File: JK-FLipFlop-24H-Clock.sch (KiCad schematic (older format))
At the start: 78 parts, among them J1 Screw_Terminal_01x02, Q1 2N3904, SW1 RESET, SW2 SET MIN, SW3 SET SEC, SW4 SET HOUR, U1 74HC109, U10 74HC00, U11 74HC00, U12 74HC00, U13 74HC00, U14 74HC00, U15 74HC00, U16 74HC00, U17 74HC109, U18 74HC109, U19 74HC109, U2 74HC109, U20 SG-3032JC, U21 74HC14, U22 74HC4040, U26 74HC4040, U3 74HC109, U4 L7805, U5 74HC109, U6 74HC109, U7 74HC109, U8 LP2950-3.0_TO92, U9 74HC109

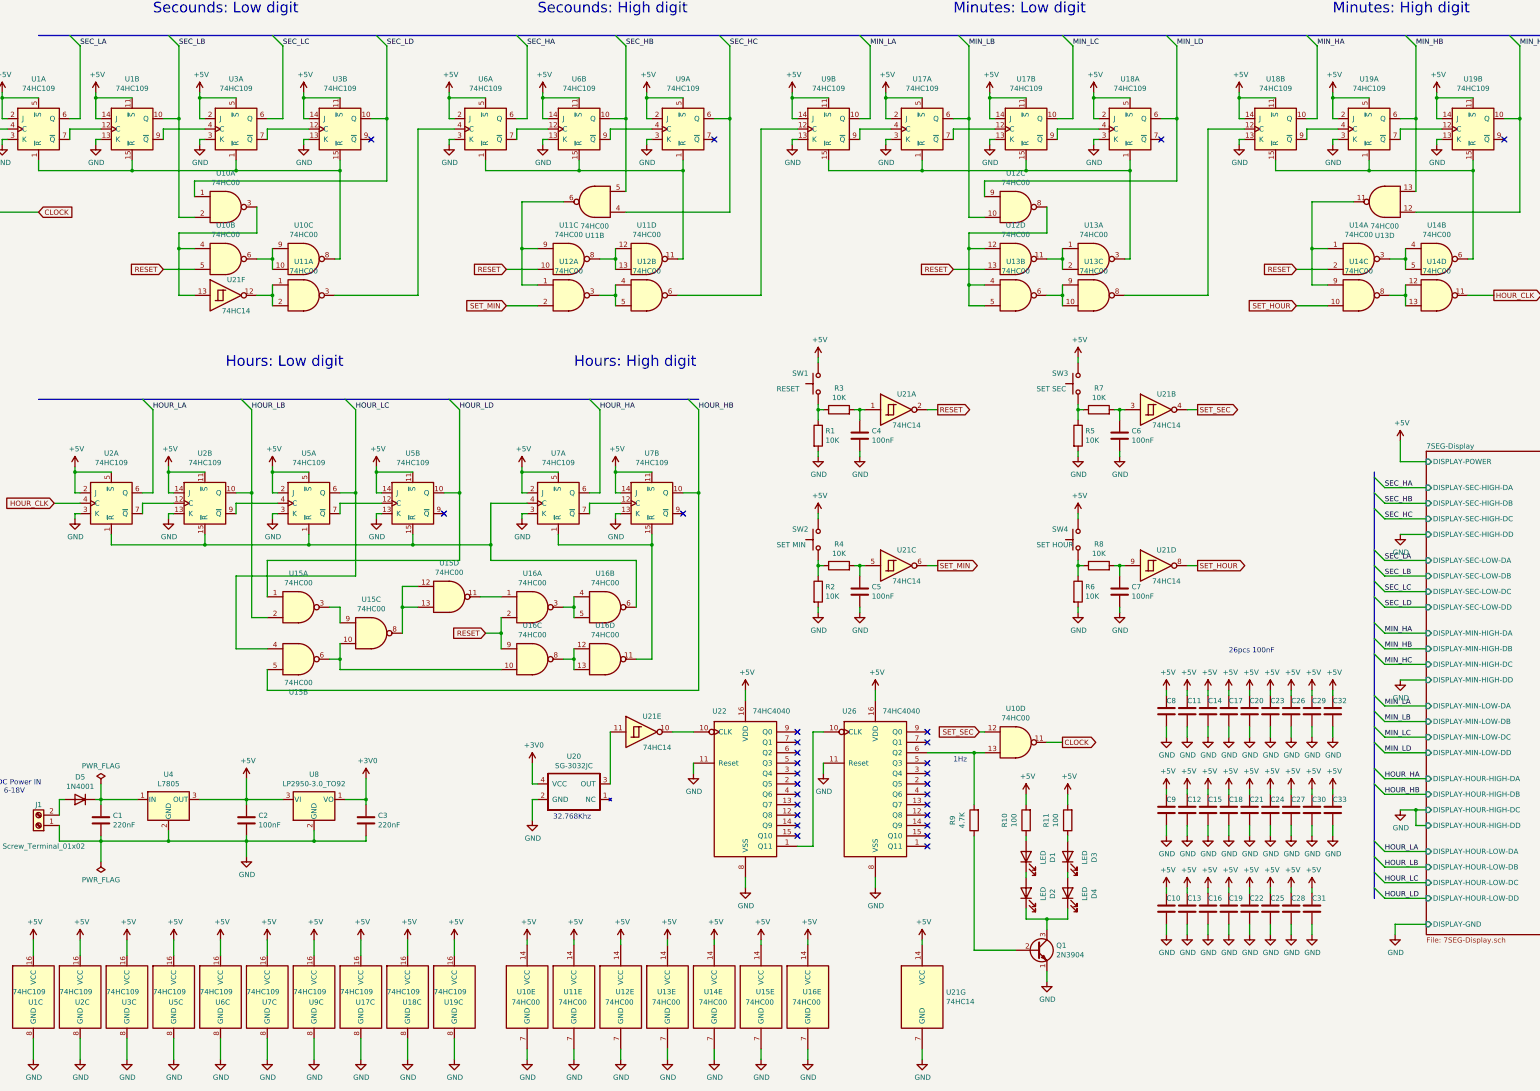
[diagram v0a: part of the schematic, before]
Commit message: Add files via upload
Error fix: HOUR digits reset and clock pulse circuit fix
Optimization: I remove one of the 74HC00
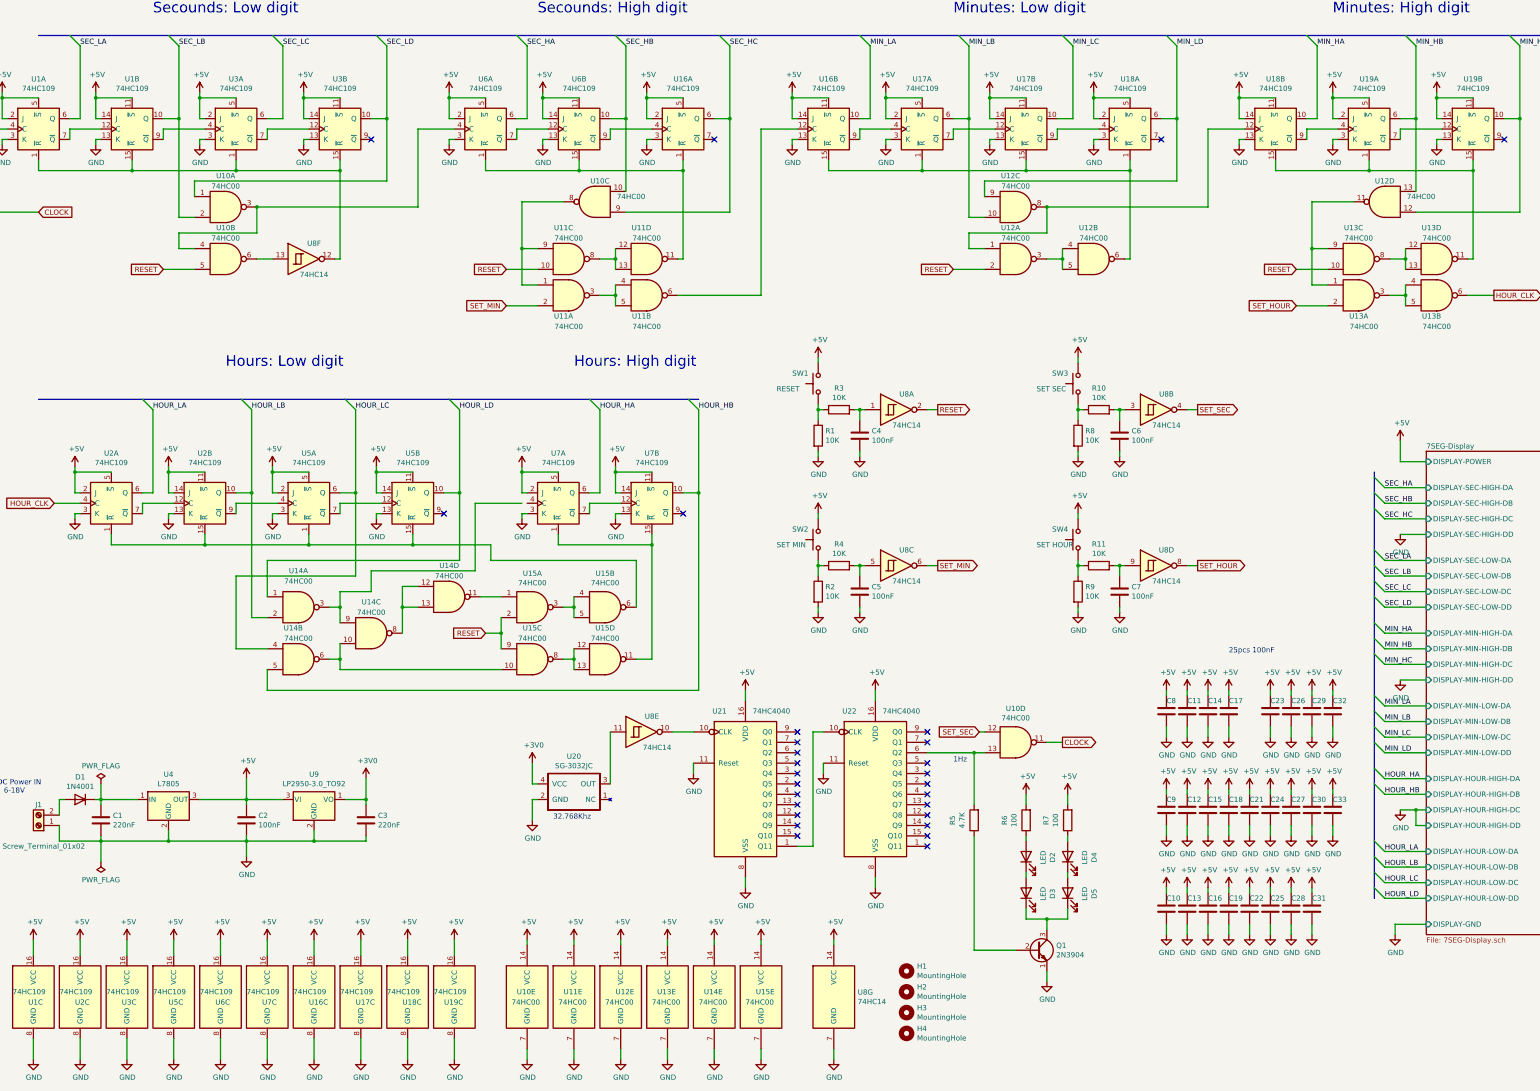
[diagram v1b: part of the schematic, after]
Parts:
- removed C20: 100nF, Capacitors_THT:C_Disc_D5.1mm_W3.2mm_P5.00mm, symbol Device:C
- removed unit 3 of U10
- removed unit 1 of U11
- removed unit 2 of U13
- removed unit 3 of U13
- removed unit 5 of U16
- added H1, H2, H3, H4: MountingHole, Mounting_Holes:MountingHole_2.2mm_M2, symbol Mechanical:MountingHole
- renumbered D5 to D1, D1 to D2, D2 to D3, D3 to D4, D4 to D5, R7 to R10, R8 to R11, R9 to R5, R10 to R6, R11 to R7, R5 to R8, R6 to R9, U11 to U10, U12 to U11, U13 to U12, U14 to U13, U15 to U14, U16 to U15, U9 to U16, U22 to U21, U26 to U22, U21 to U8, U8 to U9
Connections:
- net HOUR_CLK: now also U13.6; no longer U13.11
- net RESET: now also U12.2, U13.10; no longer U12.13, U13.2
- net SEC_HB: now also U10.10; no longer U10.5
- net SEC_HC: now also U10.9; no longer U10.4
- net SET_HOUR: now also U13.2; no longer U13.10
- net at U10.3, U10.4: now also U6.4 (C); no longer U8.13
- net at U10.6: now also U8.13
- net at U1.1 (~R), U1.15 (~R), U3.1 (~R)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: now also U8.12
- net at U16.15 (~R), U17.1 (~R), U17.15 (~R)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: now also U12.6; no longer U12.3
- net at U18.12 (C): now also U12.1, U12.8
- net at U18.15 (~R), U19.1 (~R), U19.15 (~R): now also U13.11; no longer U13.6
- net at U15.6, U2.1 (~R), U2.15 (~R)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: no longer U7.4 (C)
- net at U11.1, U11.9: now also U10.8; no longer U10.6
- new net: U12.3, U12.4, U12.5
- new net: U13.12, U13.13, U13.8
- new net: U12.11, U13.1, U13.9
- new net: U13.3, U13.4, U13.5
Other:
- note added: "25pcs 100nF"
- note removed: "26pcs 100nF"
- moved on the sheet: U8F, U8G
